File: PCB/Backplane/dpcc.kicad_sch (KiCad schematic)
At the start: 17 parts, among them Q1 Q_NMOS_GSD, U5 TPS259630, U6 AD5175

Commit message: Correct Digikey part numbers.
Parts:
- U5: DIGIKEY STOCK -> 296-TPS259631DDARCT-ND
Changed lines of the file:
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@@
 			)
 		)
-		(property "DIGIKEY" "STOCK"
+		(property "DIGIKEY" "296-TPS259631DDARCT-ND"
 			(at 105.41 38.1 0)
 			(effects

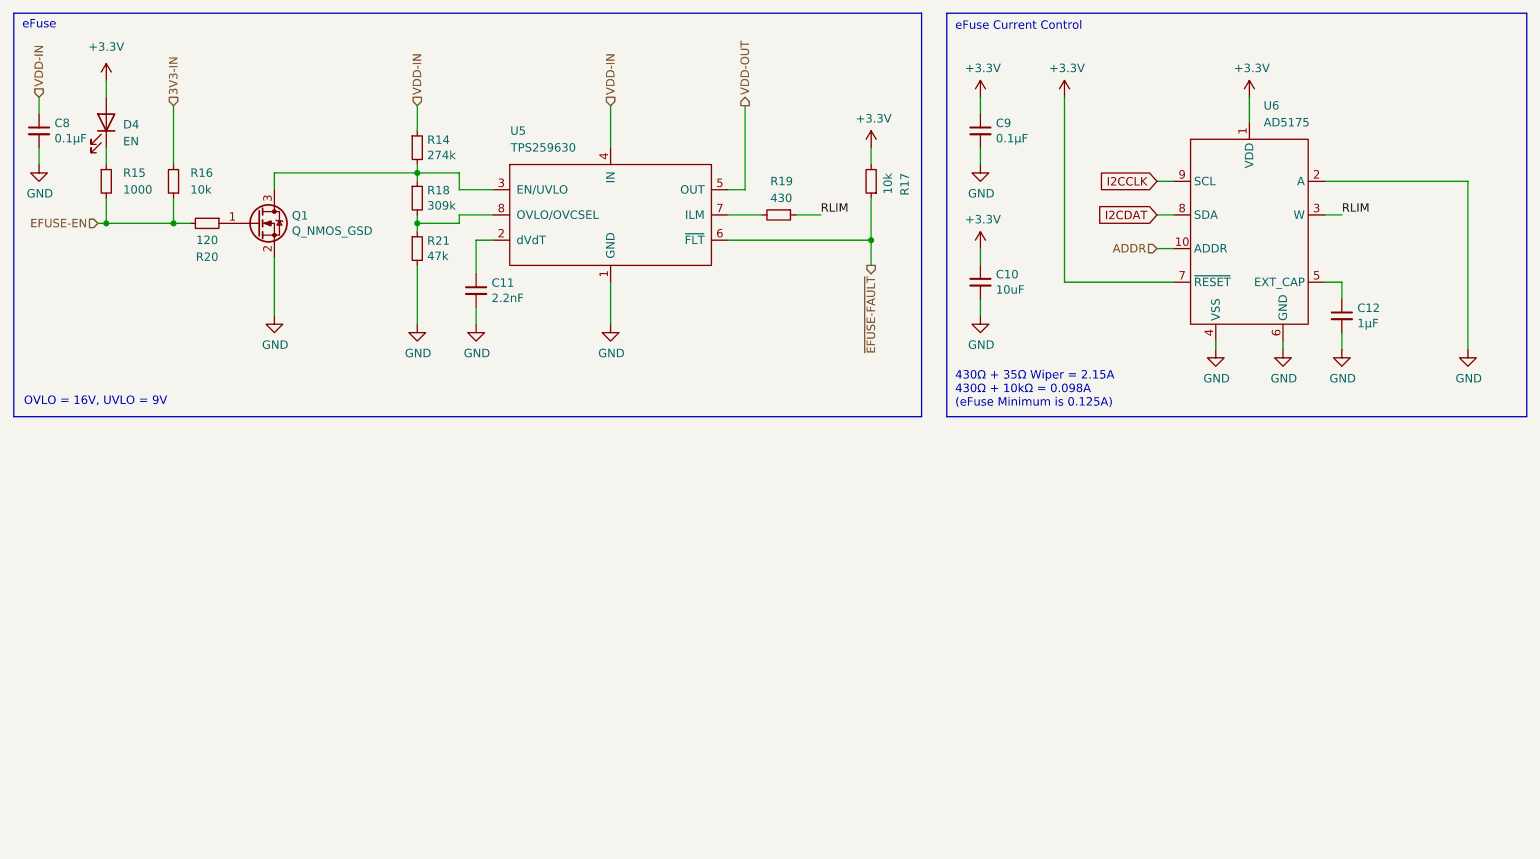
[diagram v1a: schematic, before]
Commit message: feat: Upgrade backplane to a STM32G070KB.
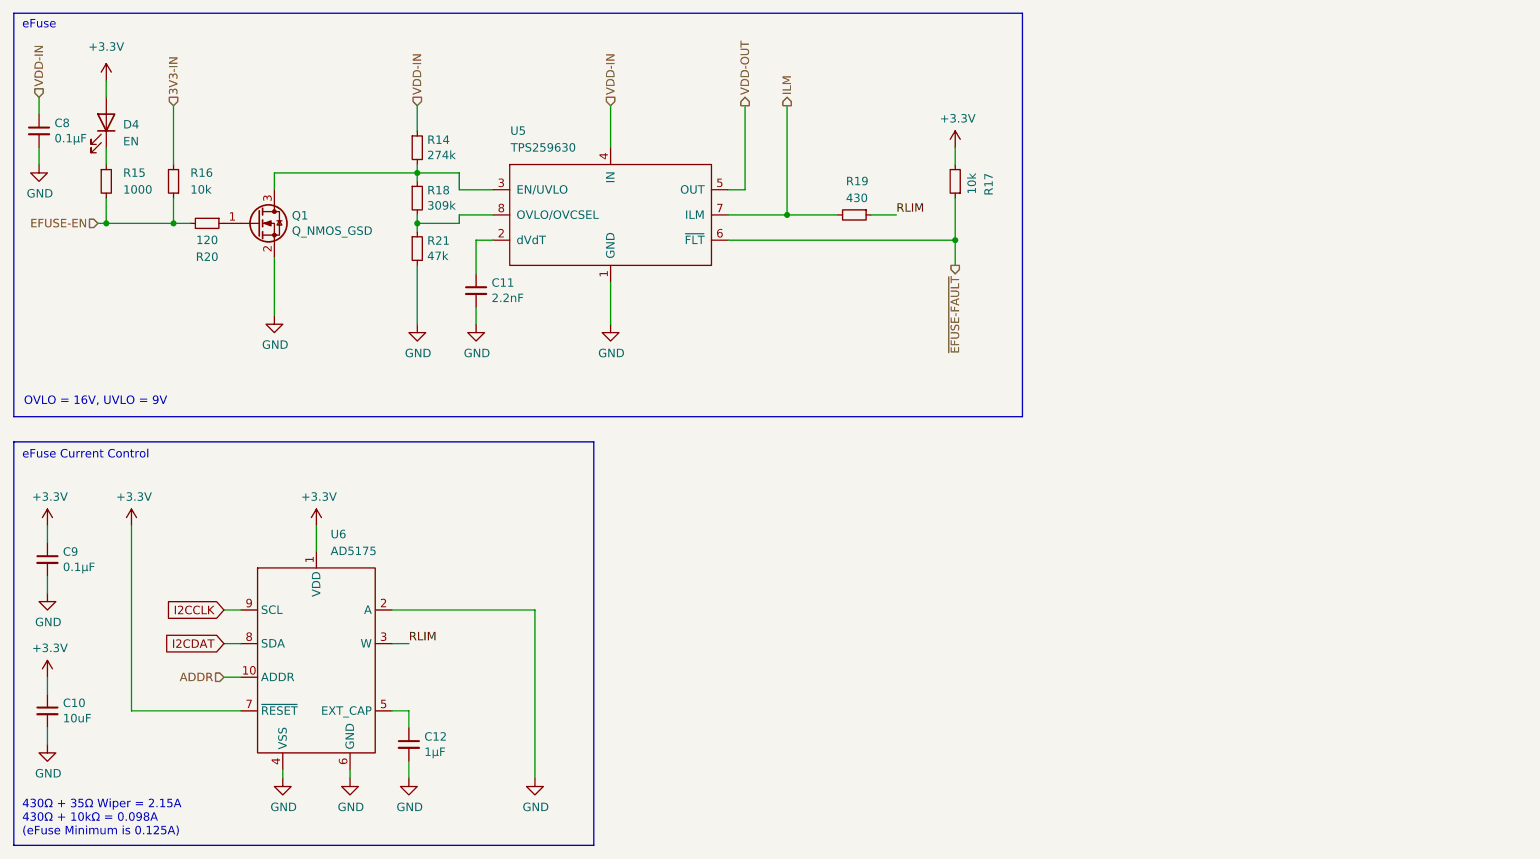
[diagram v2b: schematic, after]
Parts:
- Q1: symbol Device:Q_NMOS_GSD -> Transistor_FET:Q_NMOS_GSD
- U6: symbol KTANE:AD5175 -> KTANE:AD5175/AD5272
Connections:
- net ILM: now reaches R19.2, U5.7 (ILM)
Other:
- moved on the sheet: C10, C12, C9, R17, R19, U6
